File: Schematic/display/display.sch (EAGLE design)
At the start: 38 parts, among them IC1 74154DW, Q1 BUZ11BV, Q2 BUZ11BV, Q3 BUZ11BV, Q4 BUZ11BV, Q5 BUZ11BV, Q6 BUZ11BV, Q7 BUZ11BV, Q8 BUZ11BV, Q9 BUZ11BV

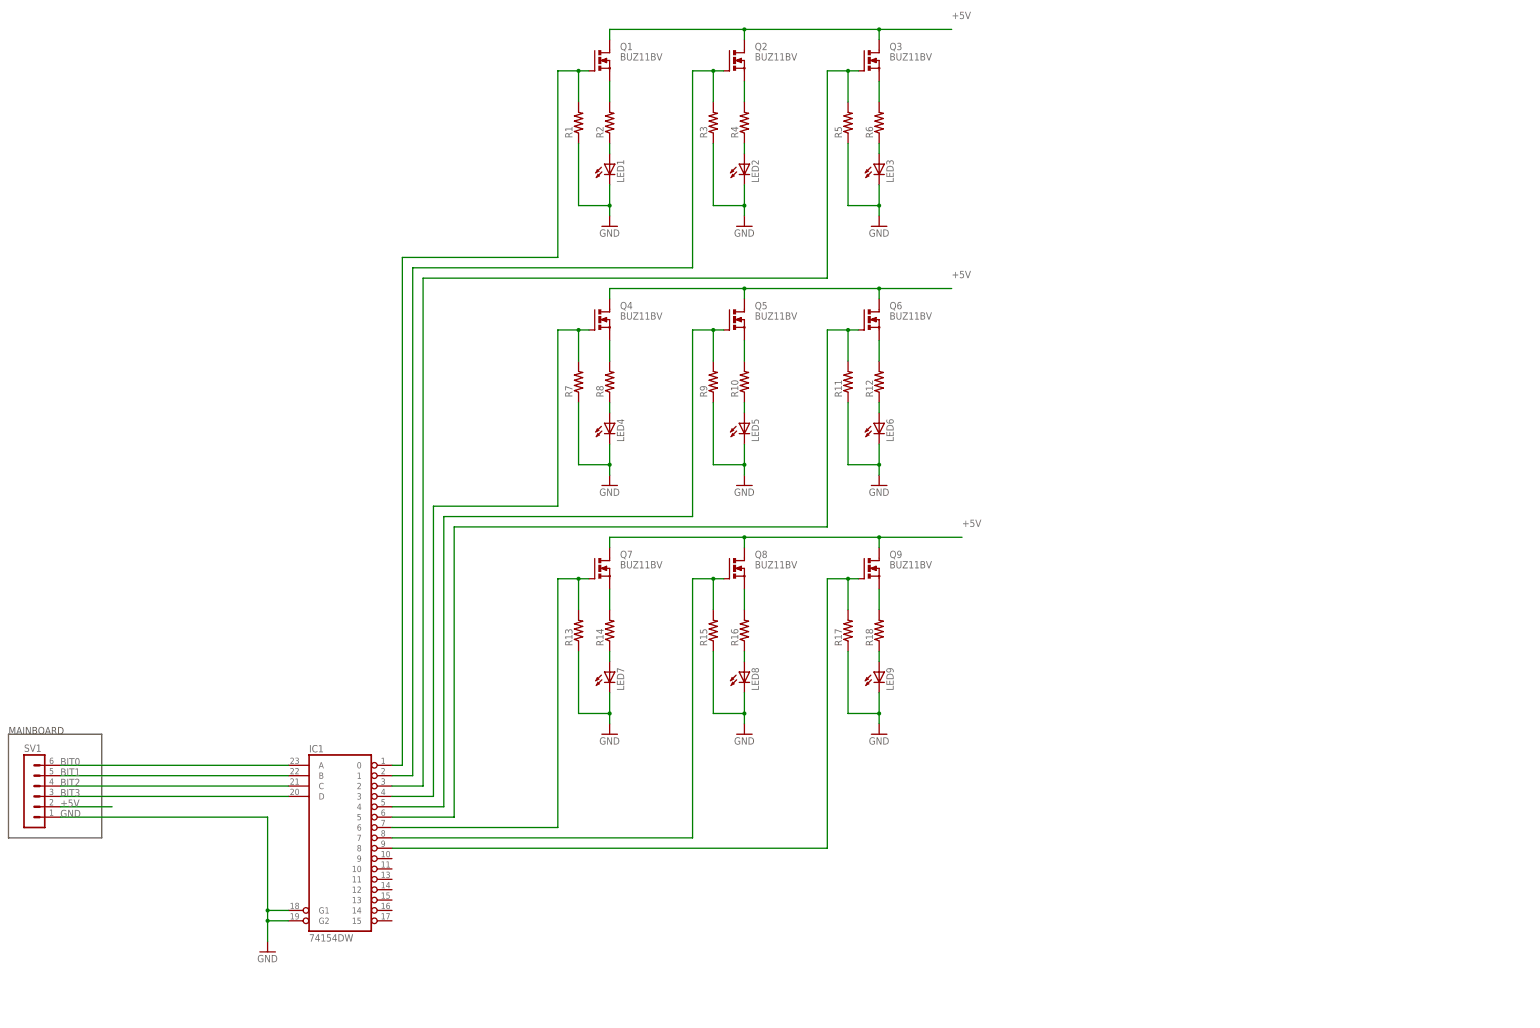
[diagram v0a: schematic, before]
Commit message: Finalized V1.0 Schematics for assignment.
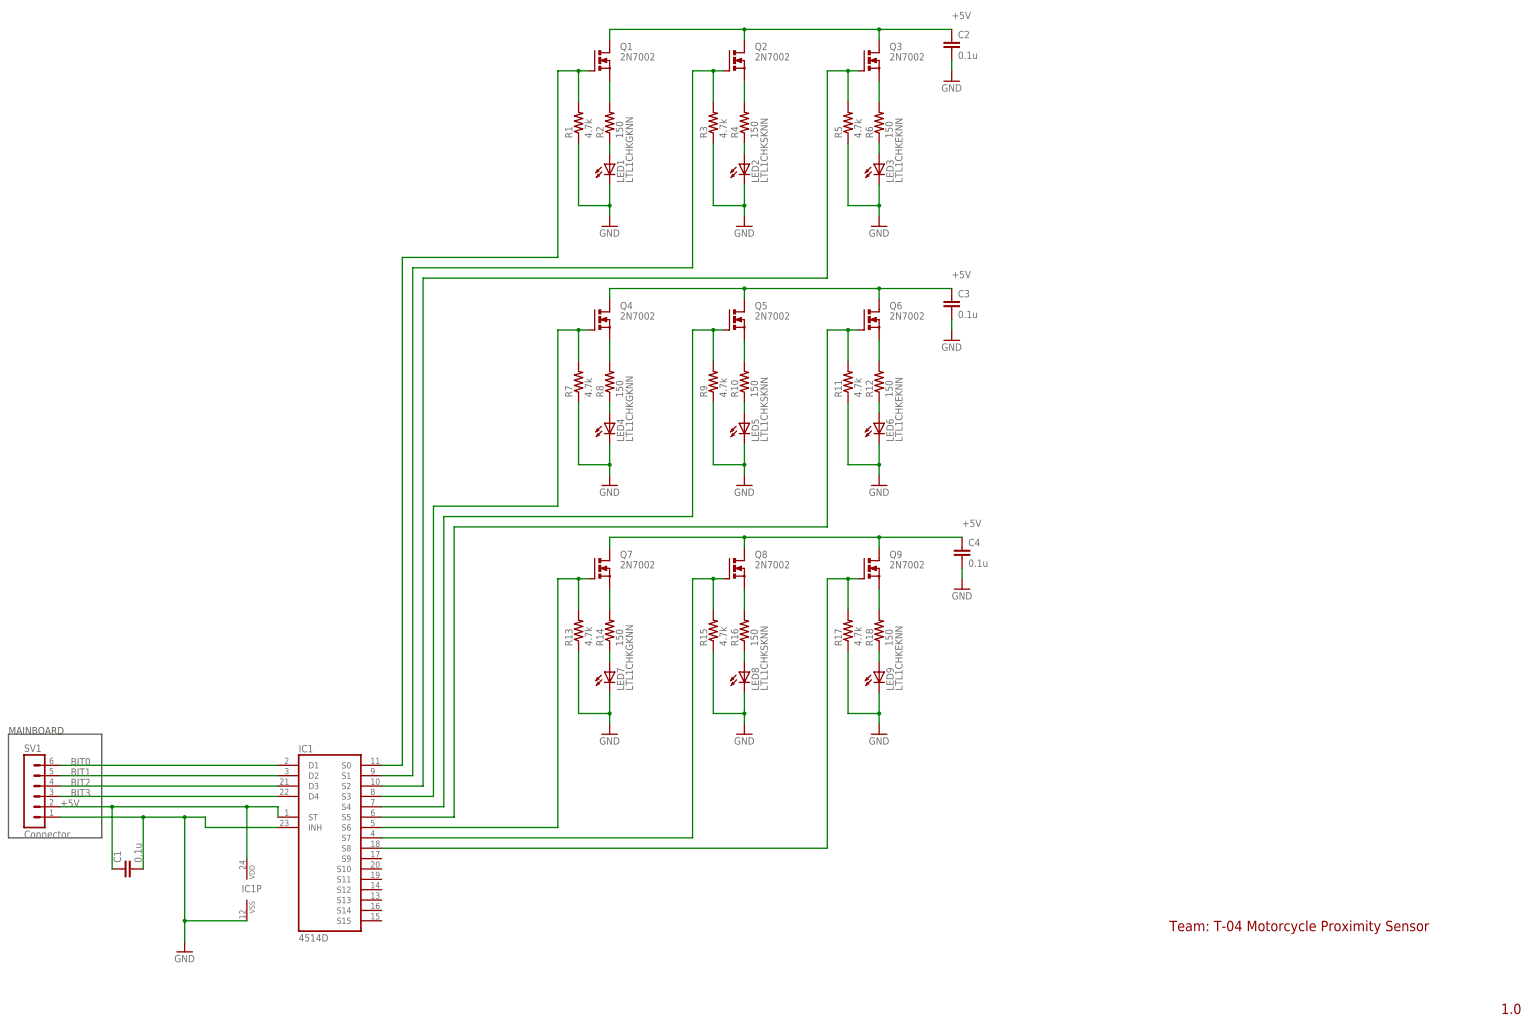
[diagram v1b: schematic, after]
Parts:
- added C1, C2, C3, C4: 0.1u, eagle-ltspice:CC3216
- IC1: value 74154DW -> 4514D; device 74xx-us:74154DW -> 45xx:4514D
- LED1, LED4, LED7: value (none) -> LTL1CHKGKNN
- LED2, LED5, LED8: value (none) -> LTL1CHKSKNN
- LED3, LED6, LED9: value (none) -> LTL1CHKEKNN
- Q1, Q2, Q3, Q4, Q5, Q6, Q7, Q8, Q9: value BUZ11BV -> 2N7002
- R1, R11, R13, R15, R17, R3, R5, R7, R9: value (none) -> 4.7k
- R10, R12, R14, R16, R18, R2, R4, R6, R8: value (none) -> 150
- SV1: value (none) -> Connector
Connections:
- net +5V: now also C1.1, C2.1, C3.1, C4.1, IC1A.ST, IC1P.VDD
- net BIT0: now also IC1A.D1; no longer IC1A.A
- net BIT1: now also IC1A.D2; no longer IC1A.B
- net BIT2: now also IC1A.D3; no longer IC1A.C
- net BIT3: now also IC1A.D4; no longer IC1A.D
- net GND: now also C1.2, C2.2, C3.2, C4.2, IC1A.INH, IC1P.VSS; no longer IC1A.G1, IC1A.G2
- net N$36: now also IC1A.S0; no longer IC1A.0
- net N$37: now also IC1A.S1; no longer IC1A.1
- net N$38: now also IC1A.S2; no longer IC1A.2
- net N$39: now also IC1A.S3; no longer IC1A.3
- net N$40: now also IC1A.S4; no longer IC1A.4
- net N$41: now also IC1A.S5; no longer IC1A.5
- net N$42: now also IC1A.S6; no longer IC1A.6
- net N$43: now also IC1A.S7; no longer IC1A.7
- net N$44: now also IC1A.S8; no longer IC1A.8
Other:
- note added: "1.0"
- note added: "Team: T-04 Motorcycle Proximity Sensor"
